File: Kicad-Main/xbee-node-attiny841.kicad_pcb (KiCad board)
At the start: 2 copper layers, 58.5 x 58.5 mm, 36 parts, among them P10 CONN_1, P11 CONN_1, P12 CONN_1, P13 CONN_1, P14 CONN_1, P15 CONN_1, P16 CONN_1, P17 CONN_1, P18 CONN_1, P2 XBee Adaptor, P3 Test, P4 Battery, P5 XBee-ext-1, P6 XBee-ext-2, P7 CONN_1, P8 CONN_1, P9 CONN_1, Q1 S1133, Q2 S9014, Q3 2N7000, U1 ATTINY84-S, U2 MAX952ESA, U3 TPS77033

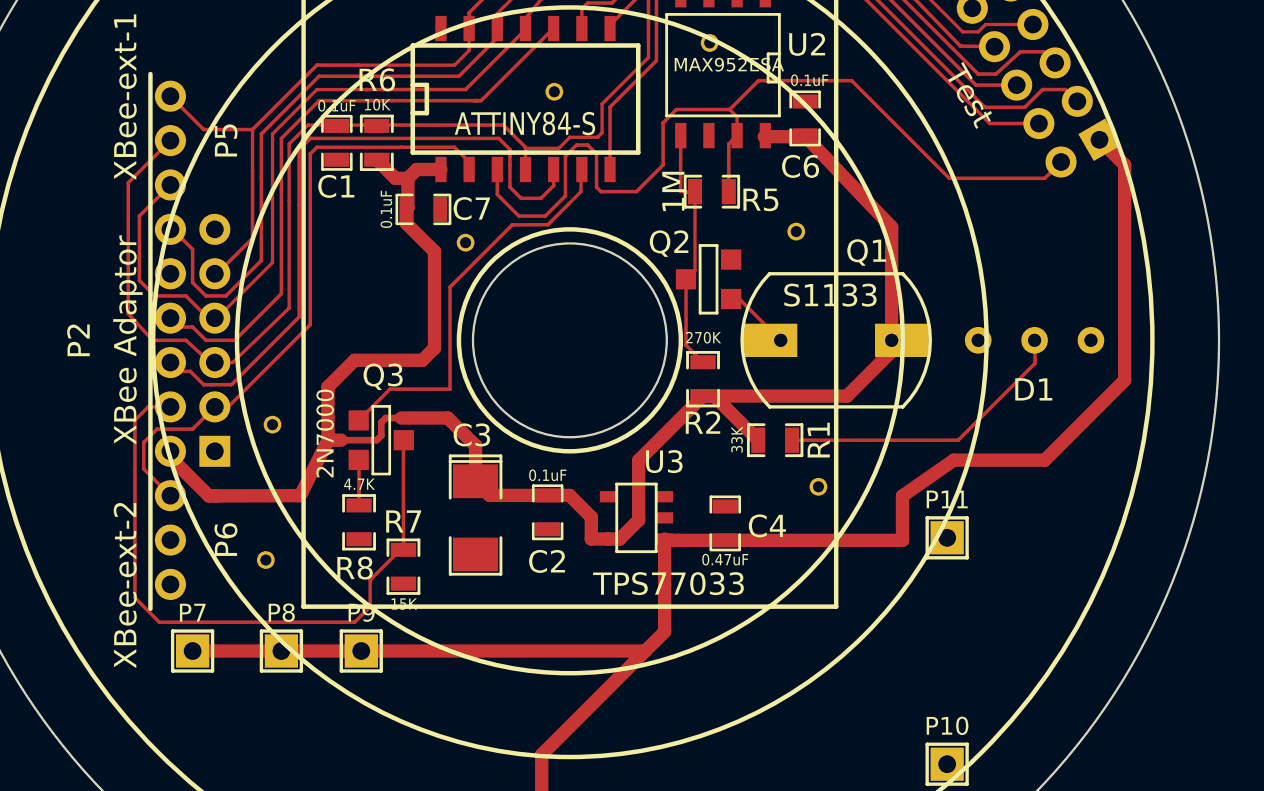
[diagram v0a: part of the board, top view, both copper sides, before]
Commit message: Correct some wiring and ground connection errors in the main board PCB. Reduce size of the LED mount to fit inside meter.
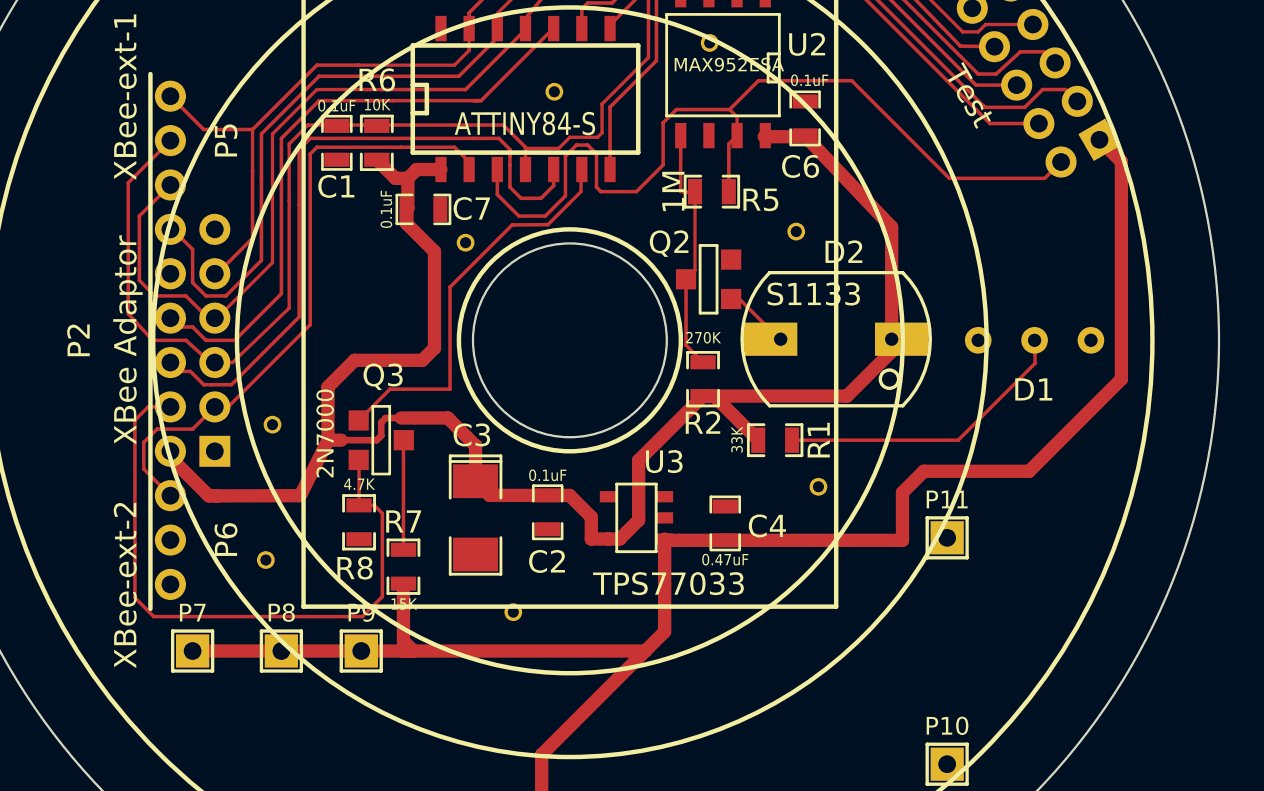
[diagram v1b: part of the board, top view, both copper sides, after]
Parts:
- removed Q1: S1133, PhotoDiode:S1133TH
- added D2: S1133, Photodiode:S1133TH, F.Cu at (212.0, 100.0)
- added Ref**: Val**, Photodiode:THROUGHVIA, F.Cu at (197.4, 112.2)
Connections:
- C4 pad 1: Net-(C4-Pad1) -> /Battery
- D1 pad 1: GND -> Net-(D1-Pad1)
- D1 pad 2: Net-(D1-Pad2) -> GND
- D1 pad 3: (no net) -> GND
- P3 pad 1: /VBatt -> /Battery
- P4 pad 1: Net-(C4-Pad1) -> /Battery
- P7 pad 1: /VBatt -> /Battery
- P8 pad 1: /VBatt -> /Battery
- P9 pad 1: /VBatt -> /Battery
- Q3 pad D: /VBatt -> Net-(Q3-PadD)
- Q3 pad S: Net-(Q3-PadS) -> /VBatt
- R1 pad 2: Net-(D1-Pad2) -> Net-(D1-Pad1)
- R7 pad 1: Net-(C4-Pad1) -> /Battery
- R7 pad 2: /VBatt -> Net-(Q3-PadD)
- R8 pad 1: Net-(Q3-PadS) -> /VBatt
- U3 pad 1: Net-(C4-Pad1) -> /Battery
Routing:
- net /Battery: track 0.00 -> 77.9 mm
- net /VBatt: track 95.5 -> 28.7 mm
- net Net-(D1-Pad2): track 13.4 -> 0.00 mm
- net Net-(D1-Pad1): track 0.00 -> 13.4 mm
- net Net-(C4-Pad1): track 8.03 -> 0.00 mm
- net Net-(Q3-PadD): track 0.00 -> 5.08 mm
- net Net-(Q3-PadS): track 2.06 -> 0.00 mm

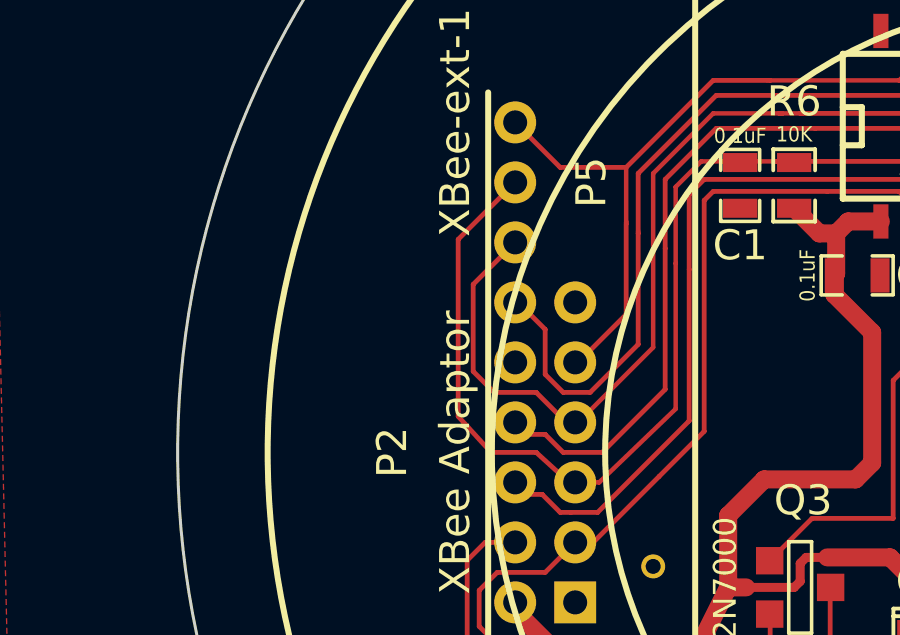
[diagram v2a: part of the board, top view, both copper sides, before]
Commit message: Main board add pulldown to XBee-sleep line.
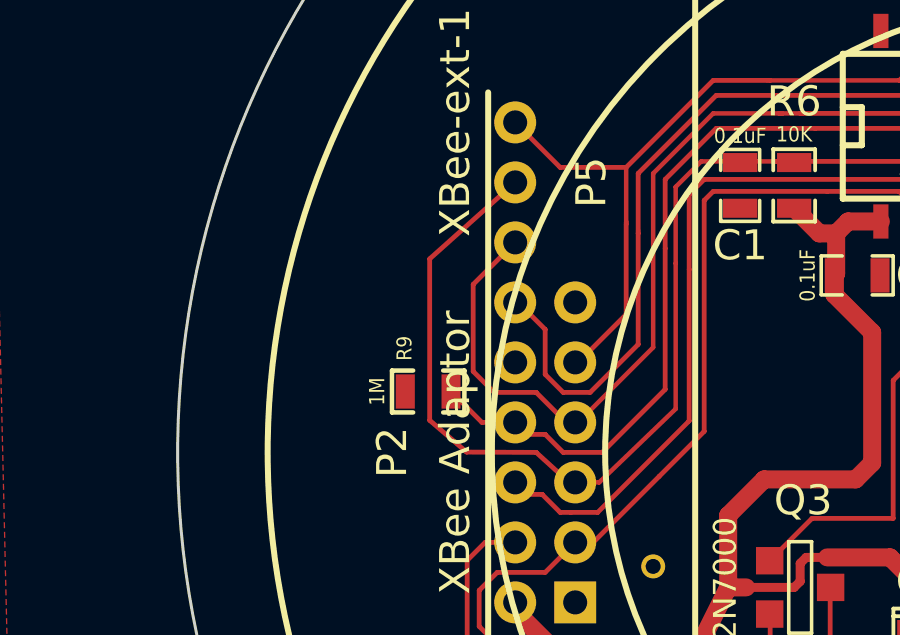
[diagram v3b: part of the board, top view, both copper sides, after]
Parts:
- added R9: 1M, SMD_Packages:SMD-0603_r, F.Cu at (179.1, 98.0)
- D1: value APD3224ZGC-F01 -> SFH4056
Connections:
- D1 pad 3: GND -> (no net)
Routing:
- net /Sleep-Rq: track 27.8 -> 30.4 mm
- net /Reset: track 73.6 -> 75.0 mm

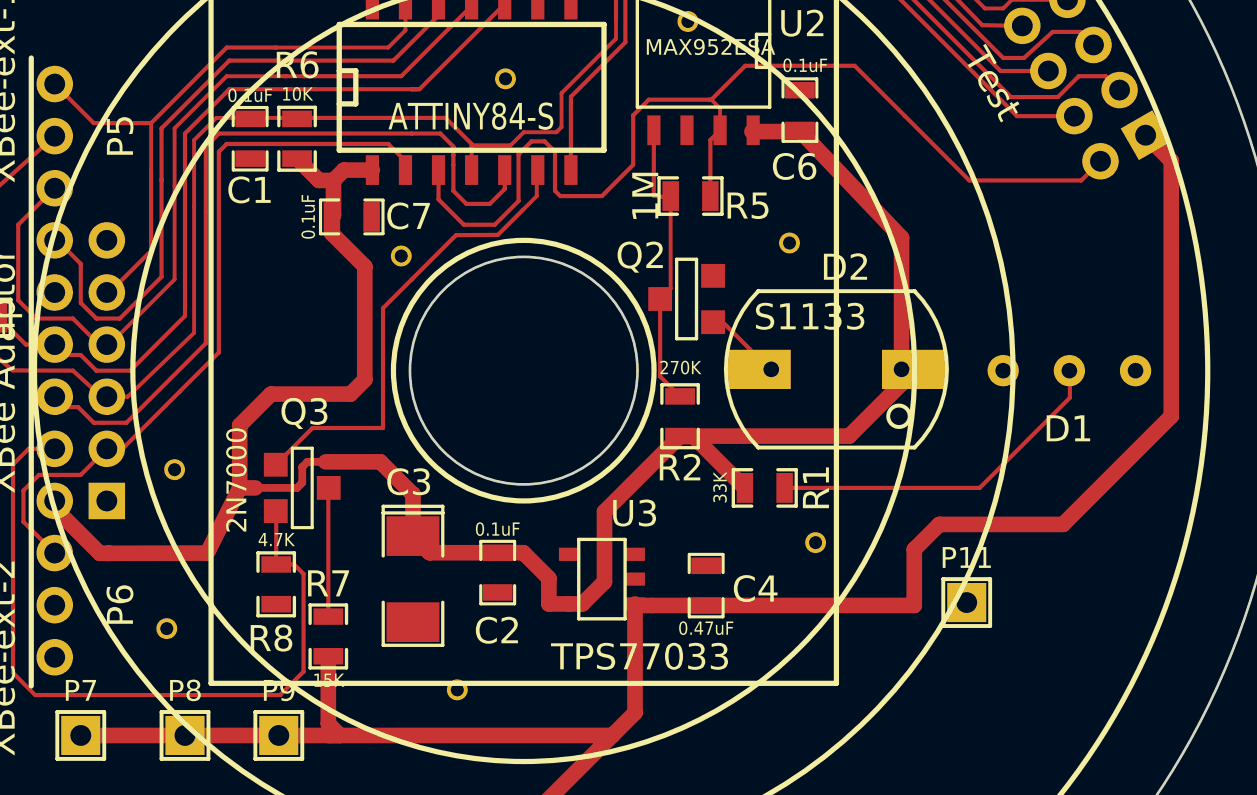
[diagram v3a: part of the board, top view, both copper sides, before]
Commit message: Update main board to filter analogue power runs and shield input signals.
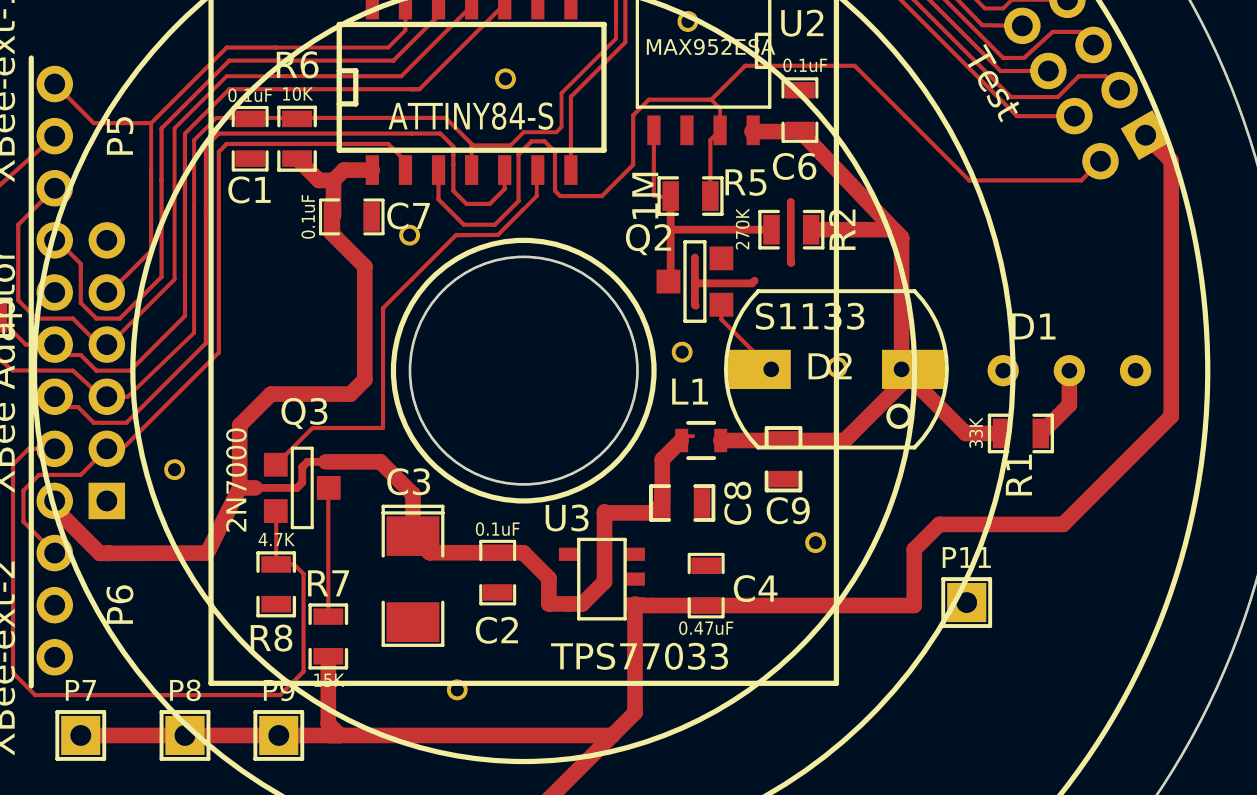
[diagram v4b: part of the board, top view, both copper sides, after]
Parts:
- added C8: , SMD_Packages:SMD-0603_c, F.Cu at (206.1, 105.1)
- added C9: , SMD_Packages:SMD-0603_c, F.Cu at (210.0, 103.4)
- added L1: , Resistors_SMD:R_0603, F.Cu at (206.8, 102.7)
- moved P17 22.4 mm to (206.1, 99.3)
- moved R1 10.0 mm to (219.1, 102.4)
- moved R2 8.34 mm to (210.3, 94.6), turned to 180 degrees
- moved P14 5.11 mm to (212.0, 99.9)
- moved P15 0.86 mm to (195.6, 94.8)
- moved Q2 0.74 mm to (206.6, 96.6)
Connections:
- D2 pad 2: VDD -> /VDDA
- R1 pad 1: VDD -> /VDDA
- R2 pad 1: VDD -> /VDDA
- U2 pad 8: VDD -> /VDDA
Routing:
- net /VDDA: track 0.00 -> 23.3 mm
- net VDD: track 80.7 -> 62.5 mm
- net Net-(D1-Pad1): track 13.4 -> 2.86 mm
- net (no net): track 0.00 -> 6.55 mm
- net Net-(Q2-Pad3): track 11.3 -> 10.7 mm

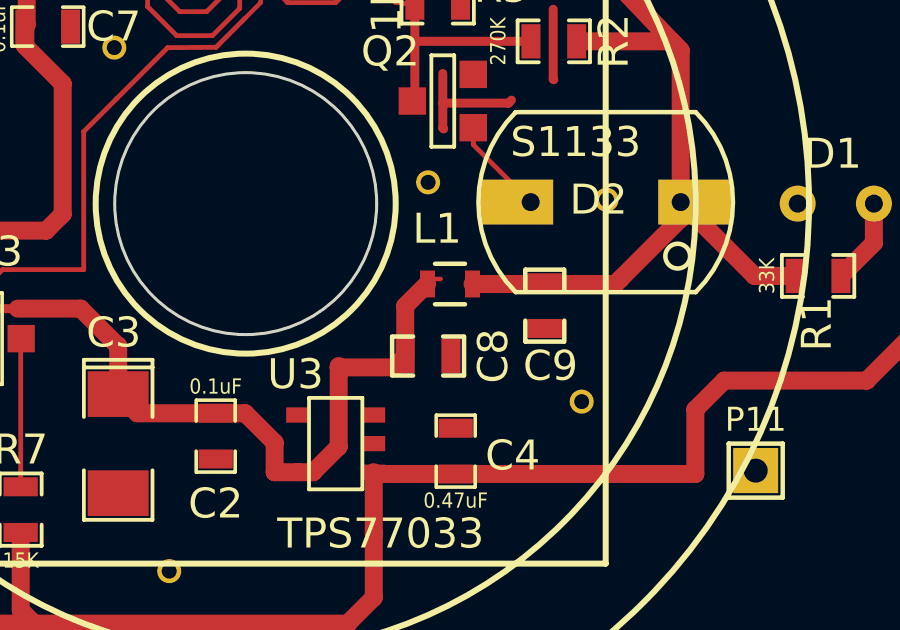
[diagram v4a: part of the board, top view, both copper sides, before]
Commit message: Minor change to board schematic to put capacitor on correct power line.
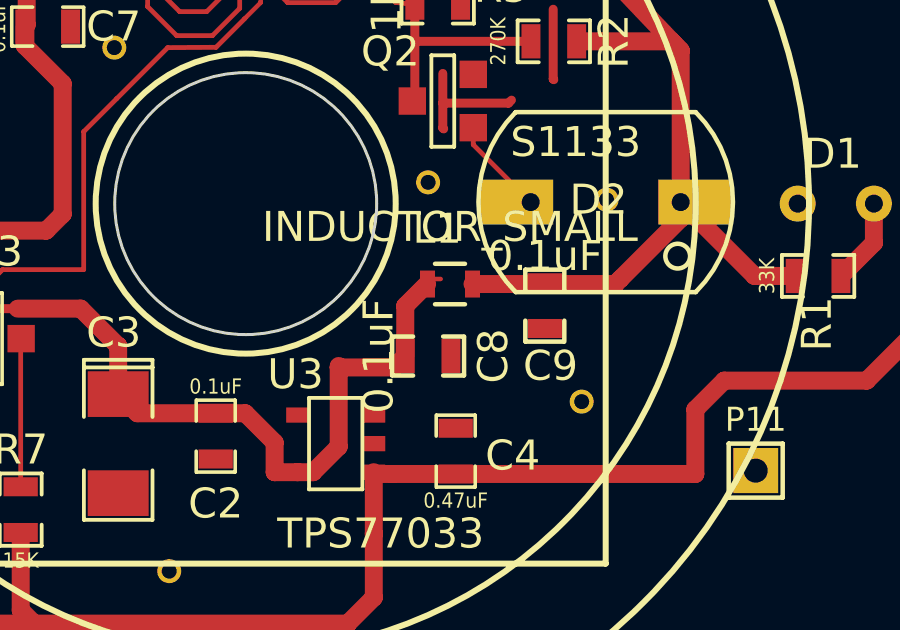
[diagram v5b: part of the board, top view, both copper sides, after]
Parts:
- C8, C9: value (none) -> 0.1uF
- L1: value (none) -> INDUCTOR_SMALL
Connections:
- C6 pad 1: VDD -> /VDDA
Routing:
- net VDD: track 62.5 -> 56.4 mm
- net /VDDA: track 23.3 -> 29.4 mm

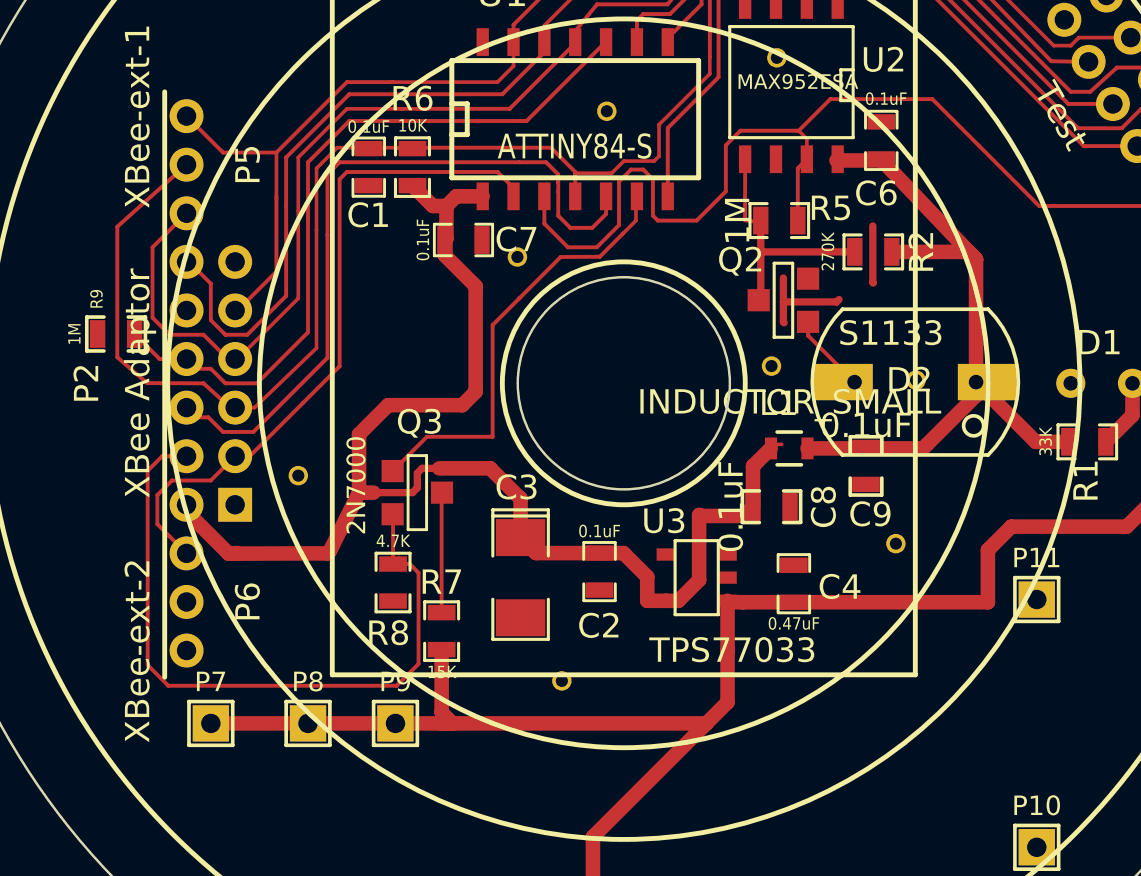
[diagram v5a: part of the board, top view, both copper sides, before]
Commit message: Main board: add a regulator for the XBee power only, plus capacitor.
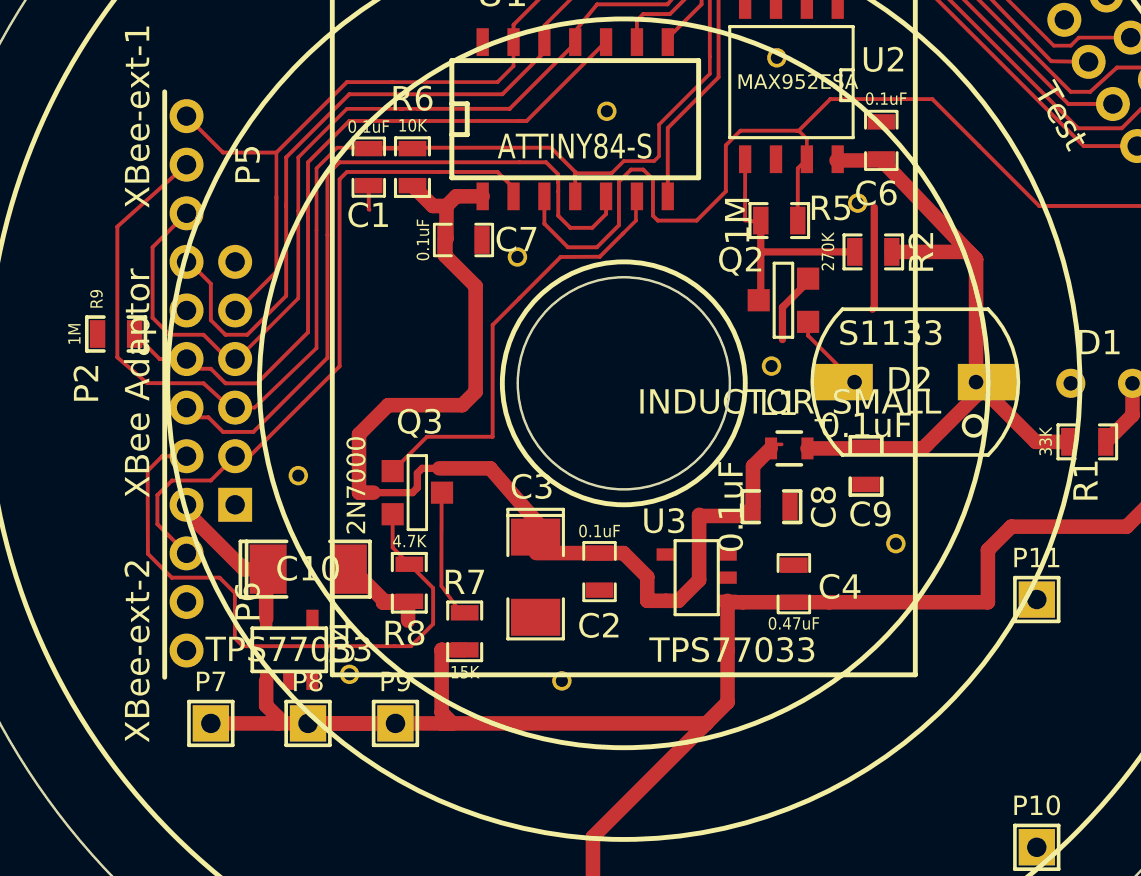
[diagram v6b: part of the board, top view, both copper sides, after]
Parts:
- added C10: 3.3uF, SMD_Packages:SMD-1206_Pol, F.Cu at (187.0, 107.7)
- added P19: CONN_1, Photodiode:THROUGHVIA, F.Cu at (209.6, 92.6)
- added U4: TPS77033, SMD_Packages:SOT-23-5, F.Cu at (186.2, 111.0)
- moved P14 26.3 mm to (188.7, 112.0)
- moved R7 0.95 mm to (193.4, 110.2)
- moved R8 0.67 mm to (191.2, 108.2)
- moved C3 0.62 mm to (196.4, 108.0)
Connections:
- P2 pad 2: VDD -> /VDDX
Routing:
- net GND: track 0.04 -> 13.4 mm
- net VDD: track 56.4 -> 45.6 mm
- net /Battery: track 77.9 -> 86.2 mm
- net /VDDX: track 0.00 -> 7.25 mm
- net (no net): track 6.55 -> 0.00 mm
- net /VBatt: track 28.7 -> 25.3 mm
- net /Reset: track 75.0 -> 77.9 mm
- net /VDDA: track 29.4 -> 31.8 mm
